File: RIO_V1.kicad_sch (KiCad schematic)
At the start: 3 parts, among them J1 Conn_01x13_Pin, U1 TinyS3_Symbol

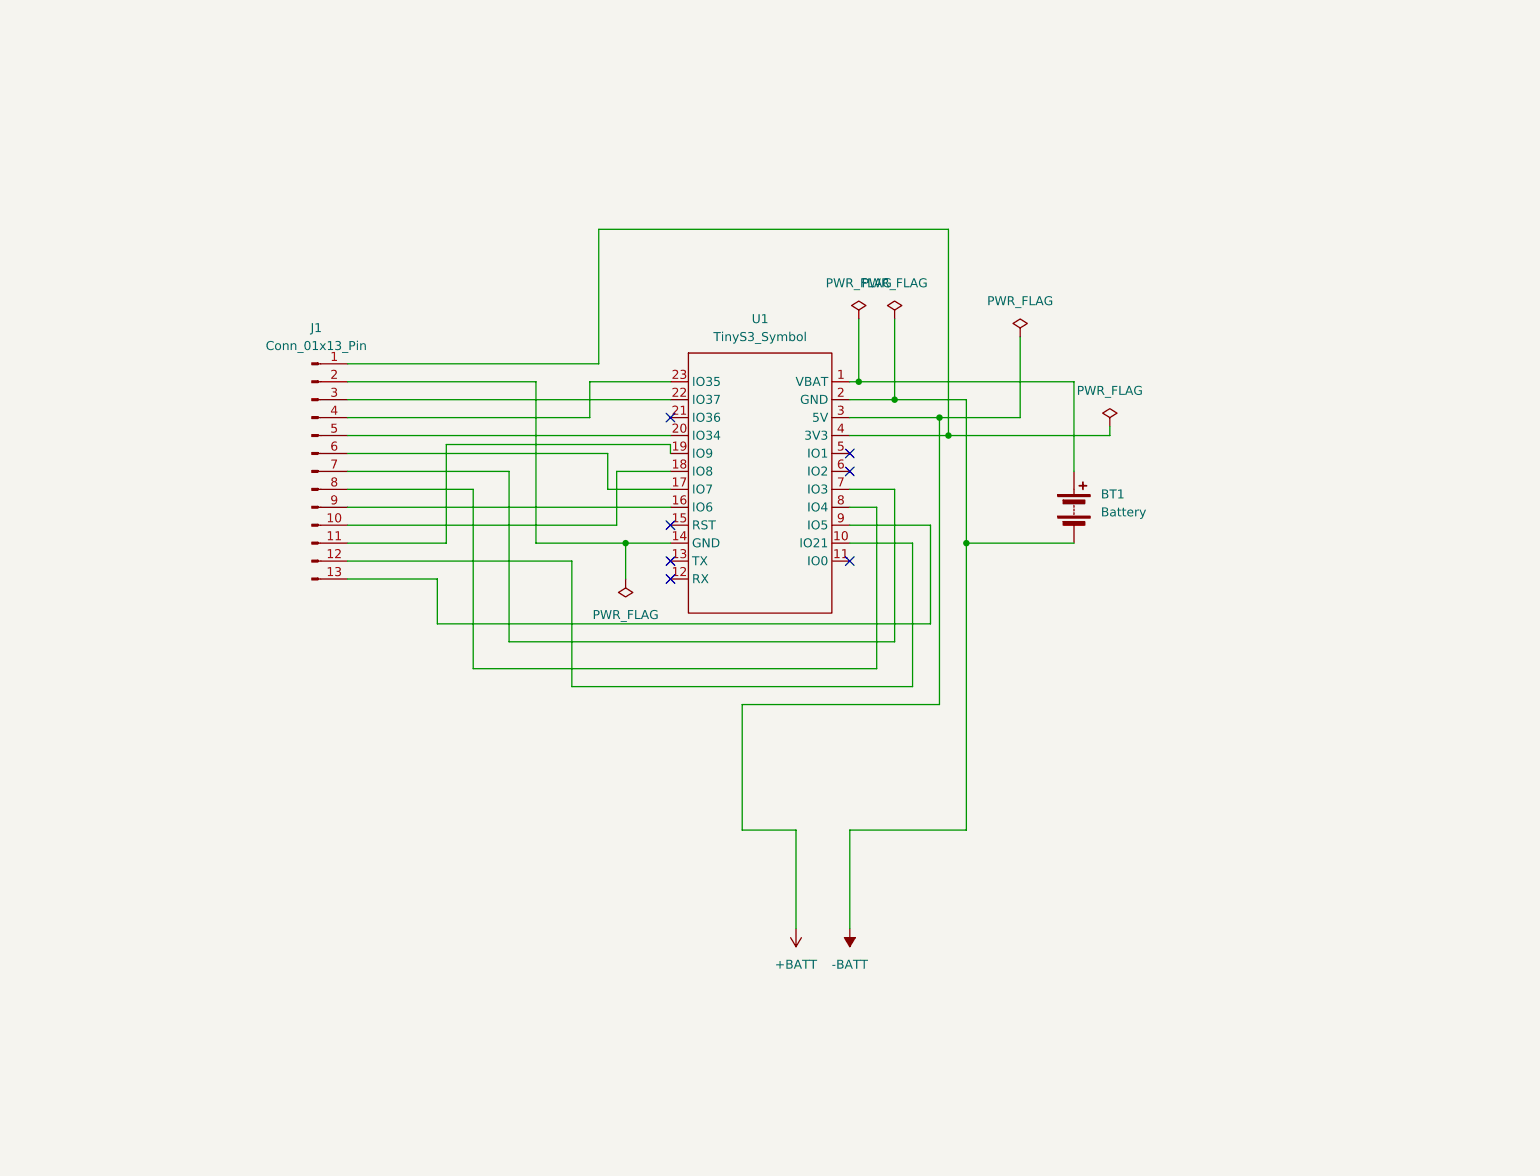
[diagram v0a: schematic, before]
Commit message: Updated Schematics & PCB To Incorporate Connector
Updated Schematic and PVB to incorporate the JST Connector instead of resodering it with a TE FPC connector
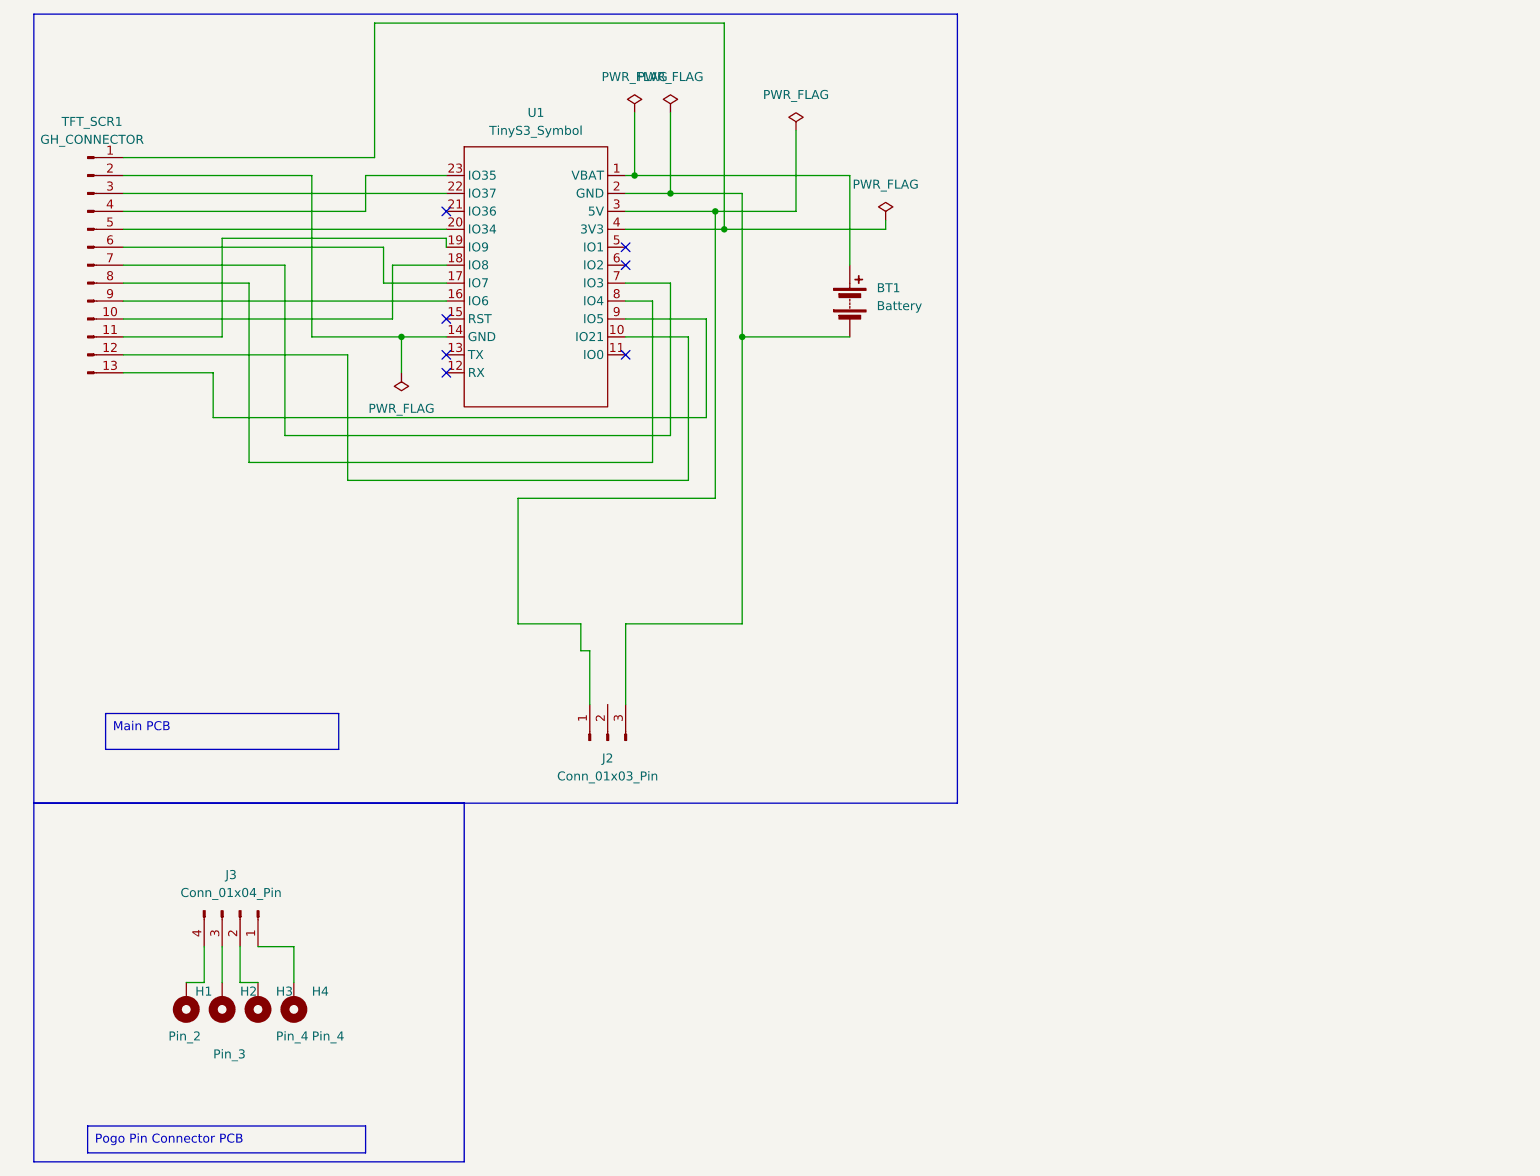
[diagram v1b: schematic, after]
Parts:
- added H1: Pin_2, MountingHole:MountingHole_2.2mm_M2_DIN965_Pad, symbol Mechanical:MountingHole_Pad
- added H2: Pin_3, MountingHole:MountingHole_2.2mm_M2_DIN965_Pad, symbol Mechanical:MountingHole_Pad
- added H3, H4: Pin_4, MountingHole:MountingHole_2.2mm_M2_DIN965_Pad, symbol Mechanical:MountingHole_Pad
- added J2: Conn_01x03_Pin, Connector_FFC-FPC:TE_84952-4_1x04-1MP_P1.0mm_Horizontal, symbol Connector:Conn_01x03_Pin
- added J3: Conn_01x04_Pin, Connector_FFC-FPC:TE_84952-4_1x04-1MP_P1.0mm_Horizontal, symbol Connector:Conn_01x04_Pin
- TFT_SCR1: renamed from J1; value Conn_01x13_Pin -> GH_CONNECTOR; footprint Connector_FFC-FPC:TE_1-84953-3_1x13-1MP_P1.0mm_Horizontal -> Connector_JST:JST_GH_BM13B-GHS-TBT_1x13-1MP_P1.25mm_Vertical
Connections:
- net +BATT: no longer names the net of U1.3 (5V)
- net +BATT: now also J2.1 (Pin_1)
- net -BATT: no longer names the net of BT1.2 (-), U1.2 (GND)
- net -BATT: now also J2.3 (Pin_3)
- new net: H2.1, J3.3 (Pin_3)
- new net: H1.1, J3.4 (Pin_4)
- new net: H4.1, J3.1 (Pin_1)
- new net: H3.1, J3.2 (Pin_2)
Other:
- company: (none) -> Akhilesh Warty
- title: (none) -> R.I.O Watch v1
- moved on the sheet: BT1, TFT_SCR1, U1

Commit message: Changed TinyS3 To NanoS3
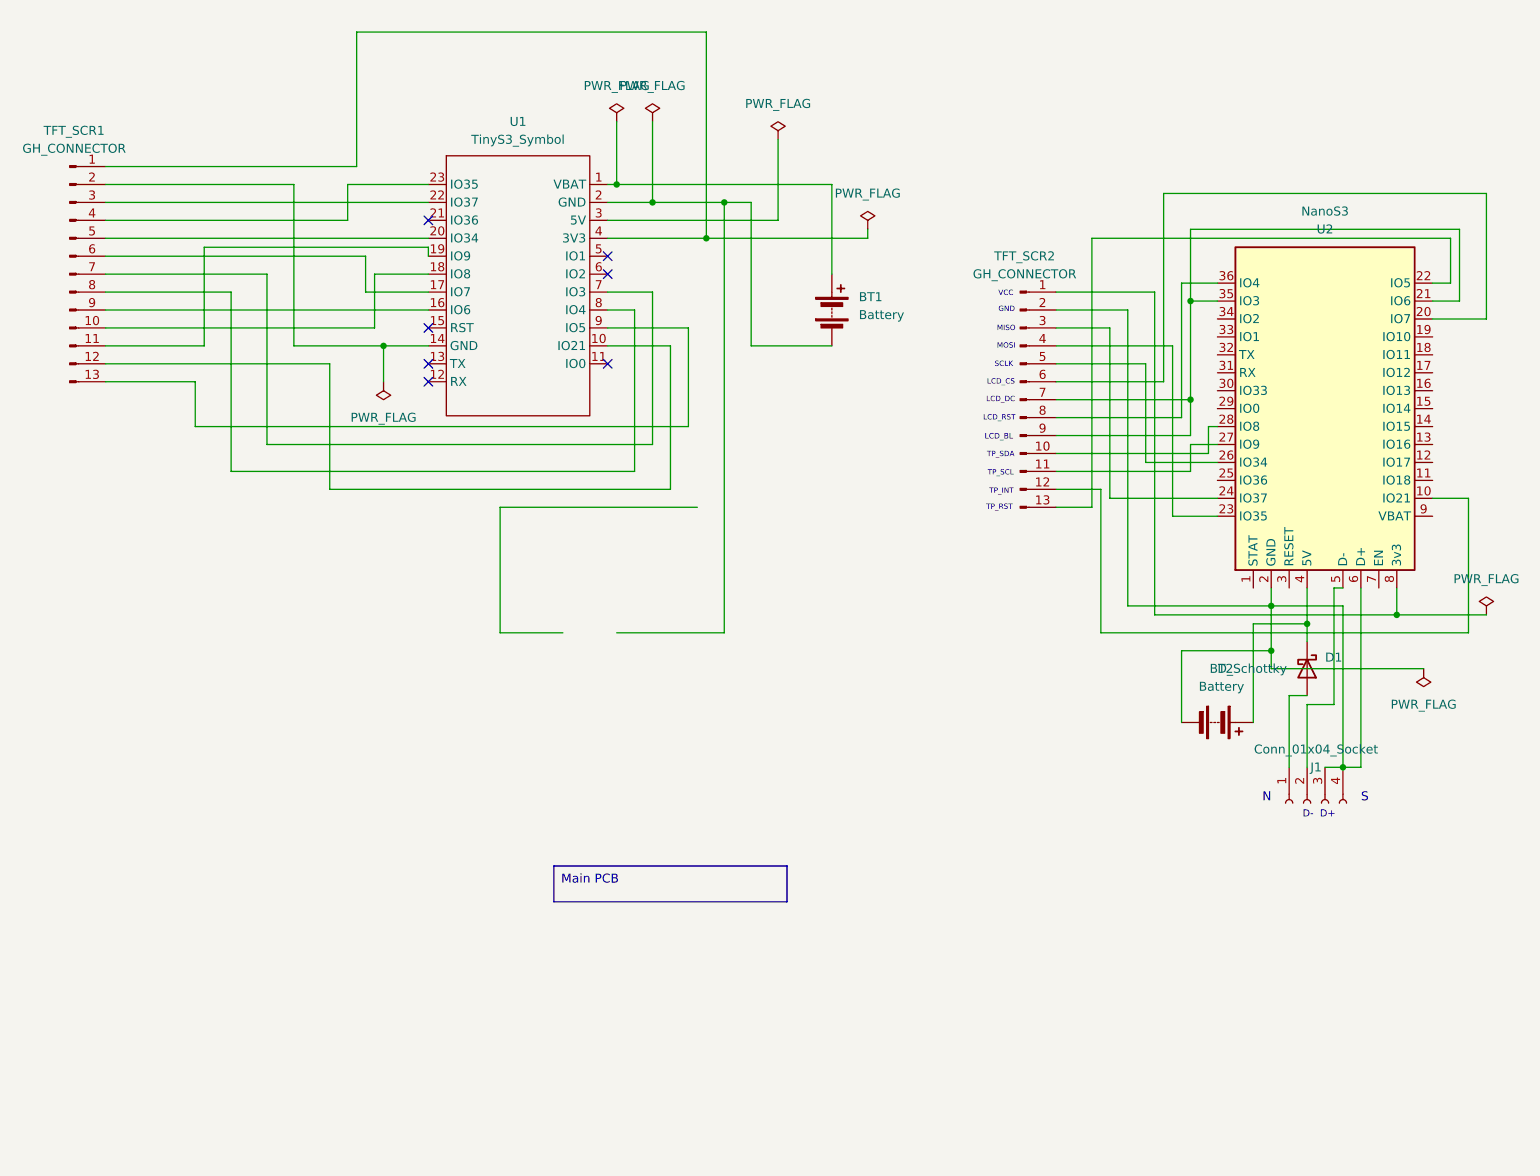
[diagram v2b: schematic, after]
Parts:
- removed H1: Pin_2, MountingHole:MountingHole_2.2mm_M2_DIN965_Pad, symbol Mechanical:MountingHole_Pad
- removed H2: Pin_3, MountingHole:MountingHole_2.2mm_M2_DIN965_Pad, symbol Mechanical:MountingHole_Pad
- removed H3, H4: Pin_4, MountingHole:MountingHole_2.2mm_M2_DIN965_Pad, symbol Mechanical:MountingHole_Pad
- removed J2: Conn_01x03_Pin, Connector_FFC-FPC:TE_84952-4_1x04-1MP_P1.0mm_Horizontal, symbol Connector:Conn_01x03_Pin
- removed J3: Conn_01x04_Pin, Connector_FFC-FPC:TE_84952-4_1x04-1MP_P1.0mm_Horizontal, symbol Connector:Conn_01x04_Pin
- added BT2: Battery, Connector_JST:JST_ACH_BM02B-ACHSS-GAN-ETF_1x02-1MP_P1.20mm_Vertical, symbol Device:Battery
- added D1: D_Schottky, Diode_SMD:D_2114_3652Metric_Pad1.85x3.75mm_HandSolder, symbol Device:D_Schottky
- added J1: Conn_01x04_Socket, Connector_FFC-FPC:TE_84952-4_1x04-1MP_P1.0mm_Horizontal, symbol Connector:Conn_01x04_Socket
- added TFT_SCR2: GH_CONNECTOR, Connector_JST:JST_GH_BM13B-GHS-TBT_1x13-1MP_P1.25mm_Vertical, symbol Connector:FPC_13_Pin
- added U2: NanoS3, NanoS3:NanoS3, symbol UnexpectedMaker:NanoS3
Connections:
- new net: BT2.1 (+), D1.1 (K), U2.4 (5V)
- new net: BT2.2 (-), J1.3 (Pin_3), J1.4 (Pin_4), TFT_SCR2.2 (Pin_2), U2.2 (GND), U2.6 (D+)
- new net: TFT_SCR2.12 (Pin_12), U2.10 (IO21)
- new net: TFT_SCR2.6 (Pin_6), U2.20 (IO7)
- new net: TFT_SCR2.7 (Pin_7), TFT_SCR2.9 (Pin_9), U2.21 (IO6), U2.35 (IO3)
- new net: TFT_SCR2.13 (Pin_13), U2.22 (IO5)
- new net: TFT_SCR2.4 (Pin_4), U2.23 (IO35)
- new net: TFT_SCR2.3 (Pin_3), U2.24 (IO37)
- new net: TFT_SCR2.5 (Pin_5), U2.26 (IO34)
- new net: TFT_SCR2.11 (Pin_11), U2.27 (IO9)
- new net: TFT_SCR2.10 (Pin_10), U2.28 (IO8)
- new net: TFT_SCR2.8 (Pin_8), U2.36 (IO4)
- new net: J1.2 (Pin_2), U2.5 (D-)
- new net: TFT_SCR2.1 (Pin_1), U2.8 (3v3)
- new net: D1.2 (A), J1.1 (Pin_1)
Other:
- note added: "D+"
- note added: "D-"
- note added: "GND"
- note added: "LCD_BL"
- note added: "LCD_CS"
- note added: "LCD_DC"
- note added: "LCD_RST"
- note added: "MISO"
- note added: "MOSI"
- note added: "N"
- note added: "S"
- note added: "SCLK"
- note added: "TP_INT"
- note added: "TP_RST"
- note added: "TP_SCL"
- note added: "TP_SDA"
- note added: "VCC"
- moved on the sheet: BT1, TFT_SCR1, U1
